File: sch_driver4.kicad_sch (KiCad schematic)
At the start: 19 parts, among them Q4 PSMN4R0-30YLDX, U14 TS5A3159ADCK, U2 ADA4099-2xR, U24 OPA333, U6 ADA4099-2xR

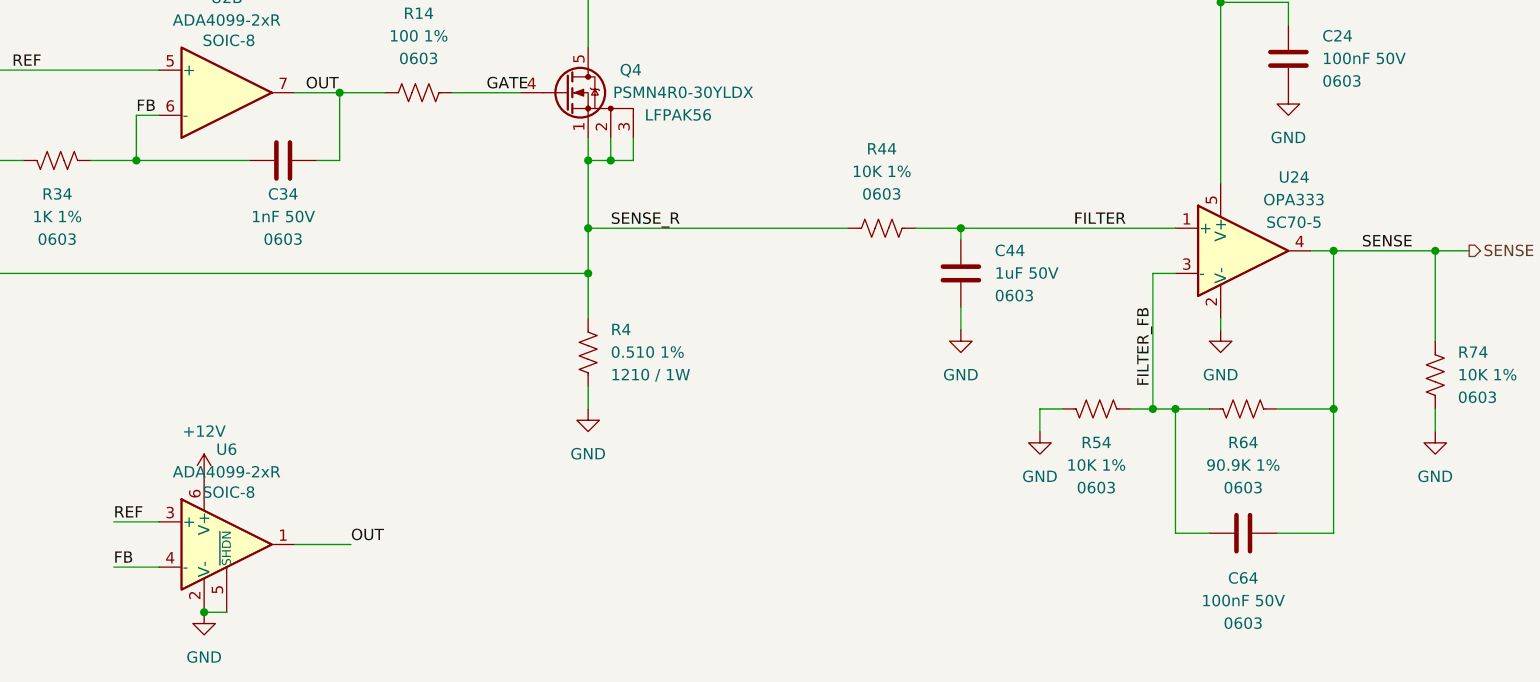
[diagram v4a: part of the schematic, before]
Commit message: Change schematic sense buffer vrom OPA333 in SC70 to OPA365 in SOT-23
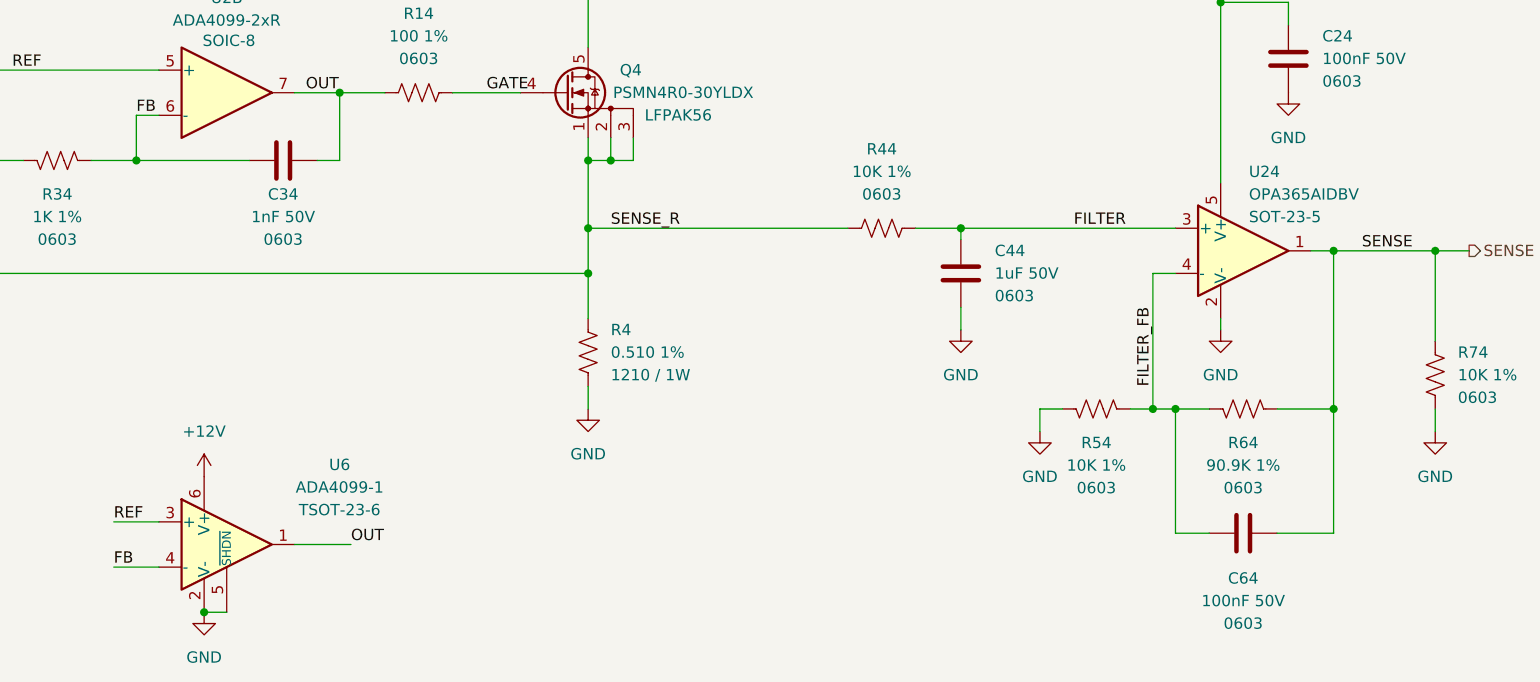
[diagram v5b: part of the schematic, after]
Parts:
- removed U24: OPA333, Package_TO_SOT_SMD:SOT-353_SC-70-5, symbol $Local:OPA333
- removed U6: ADA4099-2xR, Package_TO_SOT_SMD:TSOT-23-6, symbol Amplifier_Operational:ADA4099-1xUJ
- added U24: OPA365AIDBV, $Local:SOT-23-5, symbol $Local:OPA365AIDBV
- added U6: ADA4099-1, $Local:TSOT-23-6, symbol $Local:ADA4099-1
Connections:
- net +12V: now also U6.6 (V+)
- net +3.3V: now also U24.5 (V+)
- net FB: now also U6.4 (-)
- net FILTER: now also U24.3 (+)
- net FILTER_FB: now also U24.4 (-)
- net GND: now also U24.2 (V-), U6.2 (V-), U6.5 (~{SHDN})
- net OUT: now also U6.1
- net REF: now also U6.3 (+)
- net SENSE: now also U24.1
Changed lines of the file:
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@@
 	)
 	(junction
+		(at 99.06 111.76)
+		(diameter 0)
+		(color 0 0 0 0)
+	)
+	(junction
 		(at 118.11 177.8)
 		(diameter 0)
@@
 	)
 	(junction
-		(at 99.06 111.76)
-		(diameter 0)
-		(color 0 0 0 0)
-	)
-	(junction
 		(at 95.25 147.32)
 		(diameter 0)
@@
 	)
 	(symbol
+		(lib_id "$Local:ADA4099-1")
+		(at 101.6 104.14 0)
+		(unit 1)
+		(exclude_from_sim no)
+		(in_bom yes)
+		(on_board yes)
+		(dnp no)
+		(fields_autoplaced yes)
+		(property "Reference" "U6"
+			(at 114.3 95.1798 0)
+			(effects
+				(font
+					(size 1.27 1.27)
+				)
+			)
+		)
+		(property "Value" "ADA4099-1"
+			(at 114.3 97.7198 0)
+			(effects
+				(font
+					(size 1.27 1.27)
+				)
+			)
+		)
+		(property "Footprint" "$Local:TSOT-23-6"
+			(at 101.6 110.49 0)
+			(effects
+				(font
+					(size 1.27 1.27)
+				)
+				(hide yes)
+			)
+		)
+		(property "Datasheet" "https://www.analog.com/media/en/technical-documentation/data-sheets/ada4099-1_ada4099-2.pdf"
+			(at 101.6 113.03 0)
+			(effects
+				(font
+					(size 1.27 1.27)
+				)
+				(justify left)
+				(hide yes)
+			)
+		)
+		(property "Description" "3.15..50V supply, 8MHz GBW, Rail-to-Rail input/output, over-the-top opamp with shutdown, TSOT-6"
+			(at 101.6 104.14 0)
+			(effects
+				(font
+					(size 1.27 1.27)
+				)
+				(hide yes)
+			)
+		)
+		(property "Package" "TSOT-23-6"
+			(at 114.3 100.2598 0)
+			(effects
+				(font
+					(size 1.27 1.27)
+				)
+			)
+		)
+		(property "Digikey" "505-ADA4099-1BUJZ-RL7CT-ND"
+			(at 101.6 104.14 0)
+			(effects
+				(font
+					(size 1.27 1.27)
+				)
+				(hide yes)
+			)
+		)
+		(pin "3"
+		)
+		(pin "6"
+		)
+		(pin "1"
+		)
+		(pin "5"
+		)
+		(pin "4"
+		)
+		(pin "2"
+		)
+		(instances
+			(project "pbm_driver4_v2"
+				(path "/04797749-7aaf-42f7-a5f4-0b9aeb0ad7be/0d8fba0c-1337-4987-b588-0137eadfd0ea"
+					(reference "U6")
+					(unit 1)
+				)
+			)
+		)
+	)
+	(symbol
 		(lib_id "$Local:C")
 		(at 33.02 64.77 0)
@@
 	)
 	(symbol
+		(lib_id "$Local:OPA365AIDBV")
+		(at 215.9 71.12 0)
+		(unit 1)
+		(exclude_from_sim no)
+		(in_bom yes)
+		(on_board yes)
+		(dnp no)
+		(property "Reference" "U24"
+			(at 216.535 62.23 0)
+			(effects
+				(font
+					(size 1.27 1.27)
+				)
+				(justify left)
+			)
+		)
+		(property "Value" "OPA365AIDBV"
+			(at 216.535 64.77 0)
+			(effects
+				(font
+					(size 1.27 1.27)
+				)
+				(justify left)
+			)
+		)
+		(property "Footprint" "$Local:SOT-23-5"
+			(at 213.36 76.2 0)
+			(effects
+				(font
+					(size 1.27 1.27)
+				)
+				(justify left)
+				(hide yes)
+			)
+		)
+		(property "Datasheet" "https://www.ti.com/lit/ds/symlink/opa365.pdf"
+			(at 215.9 66.04 0)
+			(effects
+				(font
+					(size 1.27 1.27)
+				)
+				(hide yes)
+			)
+		)
+		(property "Description" "50-MHz, Zero-Crossover, Low-Distortion, High CMRR, RRI/O, Single-Supply, SOT-23-5"
+			(at 215.9 71.12 0)
+			(effects
+				(font
+					(size 1.27 1.27)
+				)
+				(hide yes)
+			)
+		)
+		(property "Package" "SOT-23-5"
+			(at 216.535 67.31 0)
+			(effects
+				(font
+					(size 1.27 1.27)
+				)
+				(justify left)
+			)
+		)
+		(property "Digikey" "296-26283-1-ND"
+			(at 215.9 71.12 0)
+			(effects
+				(font
+					(size 1.27 1.27)
+				)
+				(hide yes)
+			)
+		)
+		(pin "1"
+		)
+		(pin "5"
+		)
+		(pin "2"
+		)
+		(pin "4"
+		)
+		(pin "3"
+		)
+		(instances
+			(project "pbm_driver4_v2"
+				(path "/04797749-7aaf-42f7-a5f4-0b9aeb0ad7be/0d8fba0c-1337-4987-b588-0137eadfd0ea"
+					(reference "U24")
+					(unit 1)
+				)
+			)
+		)
+	)
+	(symbol
 		(lib_id "$Local:GND")
 		(at 193.04 91.44 0)
@@
 	)
 	(symbol
-		(lib_id "$Local:OPA333")
-		(at 215.9 71.12 0)
-		(unit 1)
-		(exclude_from_sim no)
-		(in_bom yes)
-		(on_board yes)
-		(dnp no)
-		(property "Reference" "U24"
-			(at 221.615 62.865 0)
-			(effects
-				(font
-					(size 1.27 1.27)
-				)
-			)
-		)
-		(property "Value" "OPA333"
-			(at 221.615 65.405 0)
-			(effects
-				(font
-					(size 1.27 1.27)
-				)
-			)
-		)
-		(property "Footprint" "Package_TO_SOT_SMD:SOT-353_SC-70-5"
-			(at 215.9 71.12 0)
-			(effects
-				(font
-					(size 1.27 1.27)
-				)
-				(justify left)
-				(hide yes)
-			)
-		)
-		(property "Datasheet" ""
-			(at 215.9 71.12 0)
-			(effects
-				(font
-					(size 1.27 1.27)
-				)
-				(hide yes)
-			)
-		)
-		(property "Description" "Low-Voltage Rail-to-Rail Output Operational Amplifier, SC-70-5"
-			(at 215.9 71.12 0)
-			(effects
-				(font
-					(size 1.27 1.27)
-				)
-				(hide yes)
-			)
-		)
-		(property "Package" "SC70-5"
-			(at 221.615 67.945 0)
-			(effects
-				(font
-					(size 1.27 1.27)
-				)
-			)
-		)
-		(pin "1"
-		)
-		(pin "5"
-		)
-		(pin "2"
-		)
-		(pin "3"
-		)
-		(pin "4"
-		)
-		(instances
-			(project ""
-				(path "/04797749-7aaf-42f7-a5f4-0b9aeb0ad7be/0d8fba0c-1337-4987-b588-0137eadfd0ea"
-					(reference "U24")
-					(unit 1)
-				)
-				(path "/04797749-7aaf-42f7-a5f4-0b9aeb0ad7be/4a4bbbb0-66db-4dbb-adf8-ecfc17002d21"
-					(reference "U22")
-					(unit 1)
-				)
-				(path "/04797749-7aaf-42f7-a5f4-0b9aeb0ad7be/69524e69-370d-45a1-972c-d2766add5424"
-					(reference "U21")
-					(unit 1)
-				)
-			)
-		)
-	)
-	(symbol
 		(lib_id "$Local:+3.3V")
 		(at 95.25 144.78 0)
@@
 					(unit 1)
 				)
-			)
-		)
-	)
-	(symbol
-		(lib_id "Amplifier_Operational:ADA4099-1xUJ")
-		(at 101.6 104.14 0)
-		(unit 1)
-		(exclude_from_sim no)
-		(in_bom yes)
-		(on_board yes)
-		(dnp no)
-		(property "Reference" "U6"
-			(at 101.6 93.472 0)
-			(effects
-				(font
-					(size 1.27 1.27)
-				)
-			)
-		)
-		(property "Value" "ADA4099-2xR"
-			(at 101.6 96.012 0)
-			(effects
-				(font
-					(size 1.27 1.27)
-				)
-			)
-		)
-		(property "Footprint" "Package_TO_SOT_SMD:TSOT-23-6"
-			(at 101.6 110.49 0)
-			(effects
-				(font
-					(size 1.27 1.27)
-				)
-				(hide yes)
-			)
-		)
-		(property "Datasheet" "https://www.analog.com/media/en/technical-documentation/data-sheets/ada4099-1_ada4099-2.pdf"
-			(at 101.6 113.03 0)
-			(effects
-				(font
-					(size 1.27 1.27)
-				)
-				(justify left)
-				(hide yes)
-			)
-		)
-		(property "Description" "3.15..50V supply, 8MHz GBW, Rail-to-Rail input/output, over-the-top opamp with shutdown, TSOT-6"
-			(at 101.6 104.14 0)
-			(effects
-				(font
-					(size 1.27 1.27)
-				)
-				(hide yes)
-			)
-		)
-		(property "Digikey" "505-ADA4099-2BRZ-ND"
-			(at 101.6 104.14 0)
-			(effects
-				(font
-					(size 1.27 1.27)
-				)
-				(hide yes)
-			)
-		)
-		(property "PN" "505-ADA4099-2BRZ-ND"
-			(at 101.6 104.14 0)
-			(effects
-				(font
-					(size 1.27 1.27)
-				)
-				(hide yes)
-			)
-		)
-		(property "Package" "SOIC-8"
-			(at 101.854 98.298 0)
-			(effects
-				(font
-					(size 1.27 1.27)
-				)
-			)
-		)
-		(pin "1"
-		)
-		(pin "3"
-		)
-		(pin "2"
-		)
-		(pin "6"
-		)
-		(pin "5"
-		)
-		(pin "4"
-		)
-		(instances
-			(project "pbm_driver4_v2"
-				(path "/04797749-7aaf-42f7-a5f4-0b9aeb0ad7be/0d8fba0c-1337-4987-b588-0137eadfd0ea"
-					(reference "U6")
-					(unit 1)
-				)
